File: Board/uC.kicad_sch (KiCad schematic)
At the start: 25 parts, among them U1 STM32F030K6Tx, U4 MP6612

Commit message: Schematic done.
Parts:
- C24: footprint (none) -> Capacitor_SMD:CP_Elec_8x10; REF (none) -> EEH-ZA1V101P
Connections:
- net RXD_TTL: no longer names the net of U1.25 (PA15)
- net TXD_TTL: no longer names the net of U1.24 (PA14)
- net TXEN_TTL: no longer names the net of U1.26 (PB3)
- no-connect marks 14 -> 17
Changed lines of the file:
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@@
+	)
+	(no_connect
+		(at 99.06 125.73)
 	)
 	(no_connect
@@
 	)
 	(no_connect
+		(at 68.58 110.49)
+	)
+	(no_connect
 		(at 68.58 115.57)
 	)
@@
 	(no_connect
 		(at 255.27 48.26)
+	)
+	(no_connect
+		(at 99.06 123.19)
 	)
 	(no_connect
@@
 		)
 	)
-	(global_label "RXD_TTL"
-		(shape input)
-		(at 99.06 125.73 0)
-		(fields_autoplaced yes)
-		(effects
-			(font
-				(size 1.27 1.27)
-			)
-			(justify left)
-		)
-		(property "Intersheetrefs" "${INTERSHEET_REFS}"
-			(at 109.0647 125.6506 0)
-			(effects
-				(font
-					(size 1.27 1.27)
-				)
-				(justify left)
-				(hide yes)
-			)
-		)
-	)
-	(global_label "TXD_TTL"
-		(shape output)
-		(at 99.06 123.19 0)
-		(fields_autoplaced yes)
-		(effects
-			(font
-				(size 1.27 1.27)
-			)
-			(justify left)
-		)
-		(property "Intersheetrefs" "${INTERSHEET_REFS}"
-			(at 108.7623 123.1106 0)
-			(effects
-				(font
-					(size 1.27 1.27)
-				)
-				(justify left)
-				(hide yes)
-			)
-		)
-	)
 	(global_label "HB_nFAULT"
 		(shape output)
@@
 		(property "Intersheetrefs" "${INTERSHEET_REFS}"
 			(at 216.3621 38.1 0)
-			(effects
-				(font
-					(size 1.27 1.27)
-				)
-				(justify right)
-				(hide yes)
-			)
-		)
-	)
-	(global_label "TXEN_TTL"
-		(shape output)
-		(at 68.58 110.49 180)
-		(fields_autoplaced yes)
-		(effects
-			(font
-				(size 1.27 1.27)
-			)
-			(justify right)
-		)
-		(property "Intersheetrefs" "${INTERSHEET_REFS}"
-			(at 57.0073 110.49 0)
 			(effects
 				(font
@@
 			)
 		)
-		(property "Footprint" ""
+		(property "Footprint" "Capacitor_SMD:CP_Elec_8x10"
 			(at 185.42 62.23 0)
 			(effects
@@
 			(at 185.42 62.23 0)
 			(effects
+				(font
+					(size 1.27 1.27)
+				)
+				(hide yes)
+			)
+		)
+		(property "REF" "EEH-ZA1V101P"
+			(at 185.42 62.23 0)
+			(effects

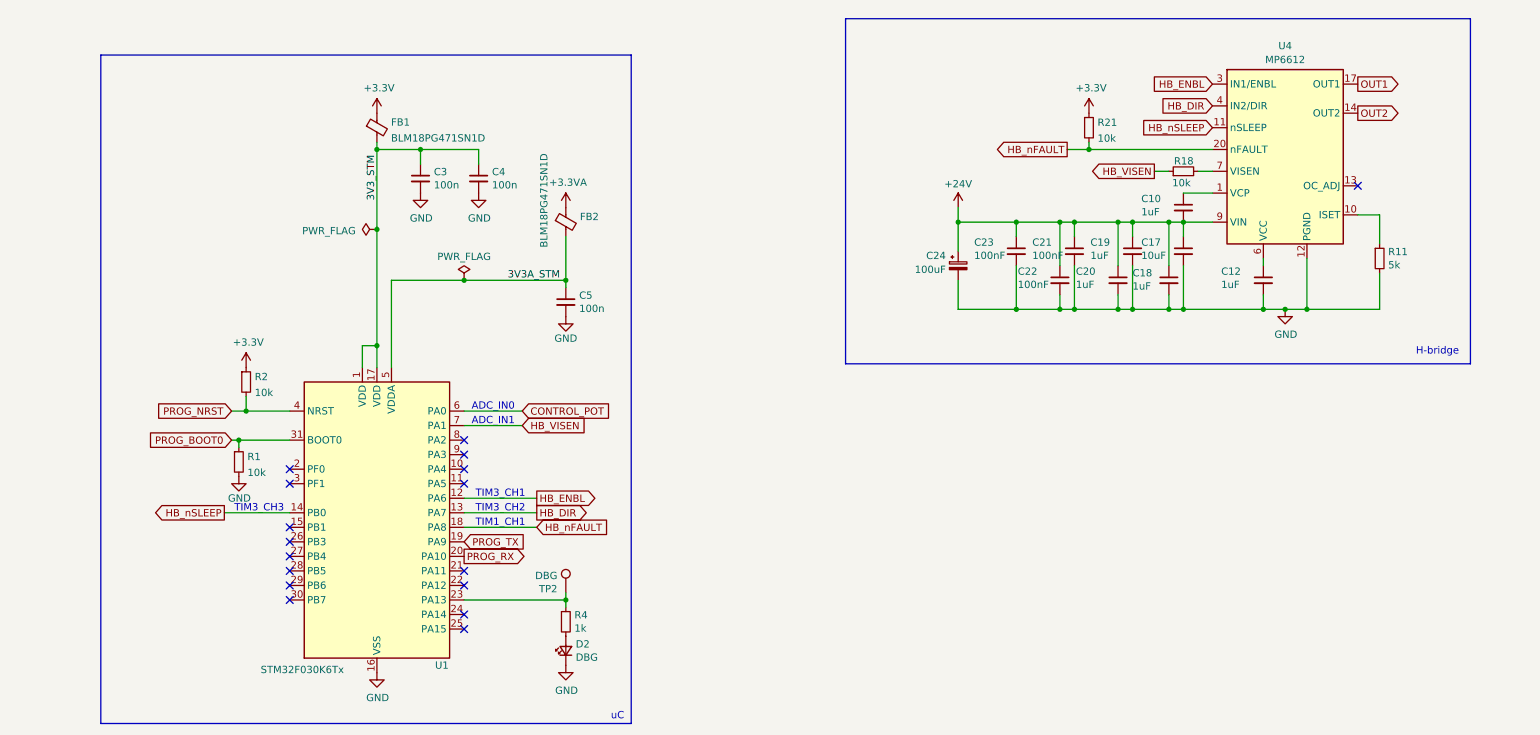
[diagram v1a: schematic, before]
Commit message: Included jdam's improvements.
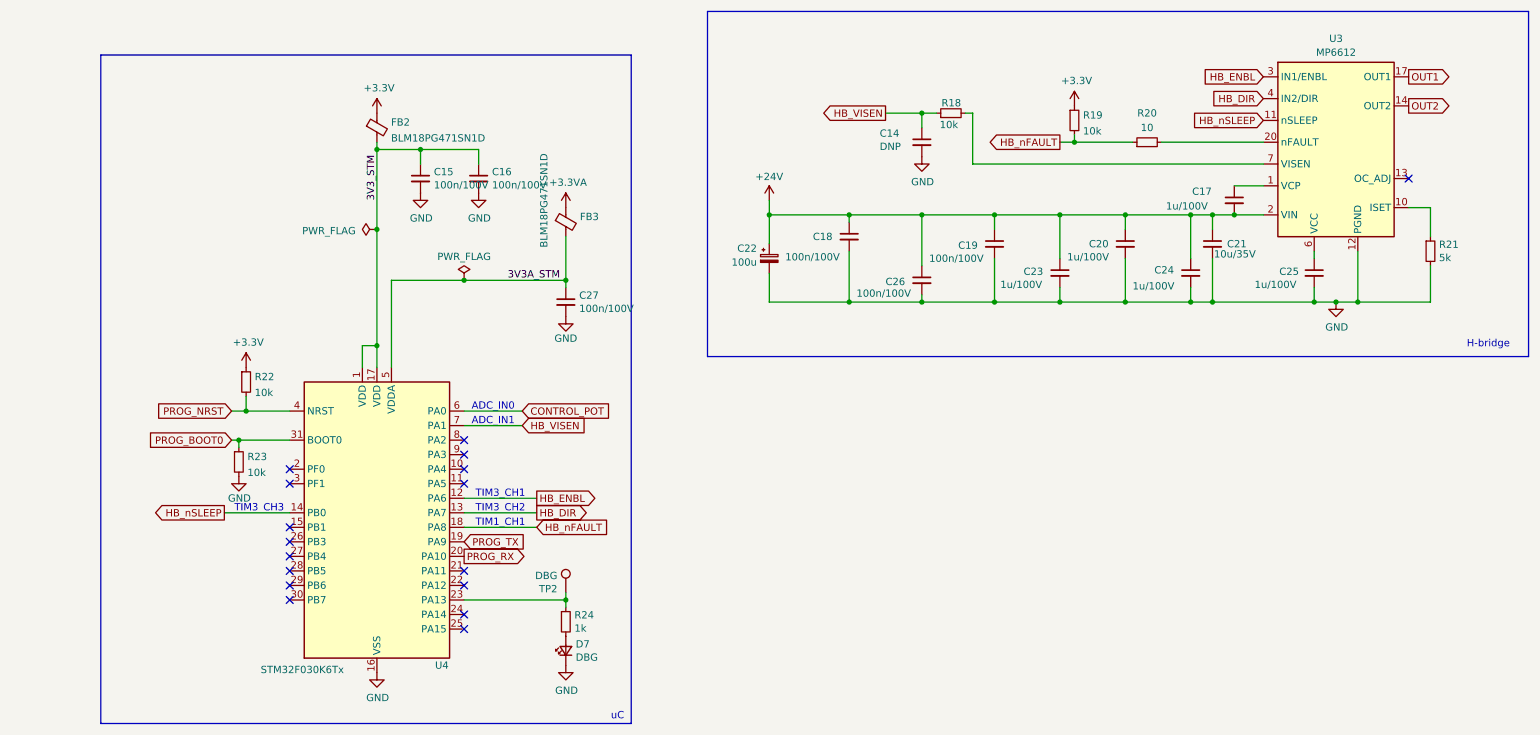
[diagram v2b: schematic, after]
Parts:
- added C14: DNP, Capacitor_SMD:C_0603_1608Metric_Pad1.08x0.95mm_HandSolder, symbol Device:C_Small
- added R20: 10, Resistor_SMD:R_0603_1608Metric_Pad0.98x0.95mm_HandSolder, symbol Device:R_Small
- C15: renamed from C3; value 100n -> 100n/100V; footprint Capacitor_SMD:C_0603_1608Metric -> Capacitor_SMD:C_0603_1608Metric_Pad1.08x0.95mm_HandSolder
- C16: renamed from C4; value 100n -> 100n/100V; footprint Capacitor_SMD:C_0603_1608Metric -> Capacitor_SMD:C_0603_1608Metric_Pad1.08x0.95mm_HandSolder
- C17: renamed from C10; value 1uF -> 1u/100V; footprint Capacitor_SMD:C_0603_1608Metric -> Capacitor_SMD:C_0603_1608Metric_Pad1.08x0.95mm_HandSolder
- C18: renamed from C23; value 100nF -> 100n/100V; footprint Capacitor_SMD:C_0603_1608Metric -> Capacitor_SMD:C_0603_1608Metric_Pad1.08x0.95mm_HandSolder
- C19: renamed from C21; value 100nF -> 100n/100V; footprint Capacitor_SMD:C_0603_1608Metric -> Capacitor_SMD:C_0603_1608Metric_Pad1.08x0.95mm_HandSolder
- C20: renamed from C19; value 1uF -> 1u/100V; footprint Capacitor_SMD:C_0603_1608Metric -> Capacitor_SMD:C_0603_1608Metric_Pad1.08x0.95mm_HandSolder
- C21: renamed from C17; value 10uF -> 10u/35V; footprint Capacitor_SMD:C_0603_1608Metric -> Capacitor_SMD:C_0603_1608Metric_Pad1.08x0.95mm_HandSolder
- C22: renamed from C24; value 100uF -> 100u
- C23: renamed from C20; value 1uF -> 1u/100V; footprint Capacitor_SMD:C_0603_1608Metric -> Capacitor_SMD:C_0603_1608Metric_Pad1.08x0.95mm_HandSolder
- C24: renamed from C18; value 1uF -> 1u/100V; footprint Capacitor_SMD:C_0603_1608Metric -> Capacitor_SMD:C_0603_1608Metric_Pad1.08x0.95mm_HandSolder
- C25: renamed from C12; value 1uF -> 1u/100V; footprint Capacitor_SMD:C_0603_1608Metric -> Capacitor_SMD:C_0603_1608Metric_Pad1.08x0.95mm_HandSolder
- C26: renamed from C22; value 100nF -> 100n/100V; footprint Capacitor_SMD:C_0603_1608Metric -> Capacitor_SMD:C_0603_1608Metric_Pad1.08x0.95mm_HandSolder
- C27: renamed from C5; value 100n -> 100n/100V; footprint Capacitor_SMD:C_0603_1608Metric -> Capacitor_SMD:C_0603_1608Metric_Pad1.08x0.95mm_HandSolder
- R18: footprint Resistor_SMD:R_0603_1608Metric -> Resistor_SMD:R_0603_1608Metric_Pad0.98x0.95mm_HandSolder
- R19: renamed from R21; footprint Resistor_SMD:R_0603_1608Metric -> Resistor_SMD:R_0603_1608Metric_Pad0.98x0.95mm_HandSolder
- R21: renamed from R11; footprint Resistor_SMD:R_0603_1608Metric -> Resistor_SMD:R_0603_1608Metric_Pad0.98x0.95mm_HandSolder
- R22: renamed from R2; footprint Resistor_SMD:R_0603_1608Metric -> Resistor_SMD:R_0603_1608Metric_Pad0.98x0.95mm_HandSolder
- R23: renamed from R1; footprint Resistor_SMD:R_0603_1608Metric -> Resistor_SMD:R_0603_1608Metric_Pad0.98x0.95mm_HandSolder
- R24: renamed from R4; footprint Resistor_SMD:R_0603_1608Metric -> Resistor_SMD:R_0603_1608Metric_Pad0.98x0.95mm_HandSolder
- renumbered D2 to D7, FB1 to FB2, FB2 to FB3, U4 to U3, U1 to U4
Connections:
- net HB_VISEN: now also C14.1
- net HB_nFAULT: now also R20.1; no longer U3.20 (nFAULT)
- net AGND renamed GND
- net GND: now also C14.2
- new net: R20.2, U3.20 (nFAULT)
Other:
- moved on the sheet: C17, C18, C19, C20, C21, C22, C23, C24, C25, C26, R18, R19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

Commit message: WIP on routing
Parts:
- removed D7: DBG, LED_SMD:LED_0603_1608Metric, symbol Device:LED_Small
- removed R24: 1k, Resistor_SMD:R_0603_1608Metric_Pad0.98x0.95mm_HandSolder, symbol Device:R_Small
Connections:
- net HB_VISEN: now also U4.8 (PA2); no longer U4.7 (PA1)
- net STATUS_LED: now reaches TP2.1, U4.23 (PA13)
- new net POSITION_POT: U4.7 (PA1)
- no-connect marks 17 -> 16
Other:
- note added: "ADC_IN2"
- moved on the sheet: C15, C16, C27, FB2, FB3, R22, R23, TP2, U4

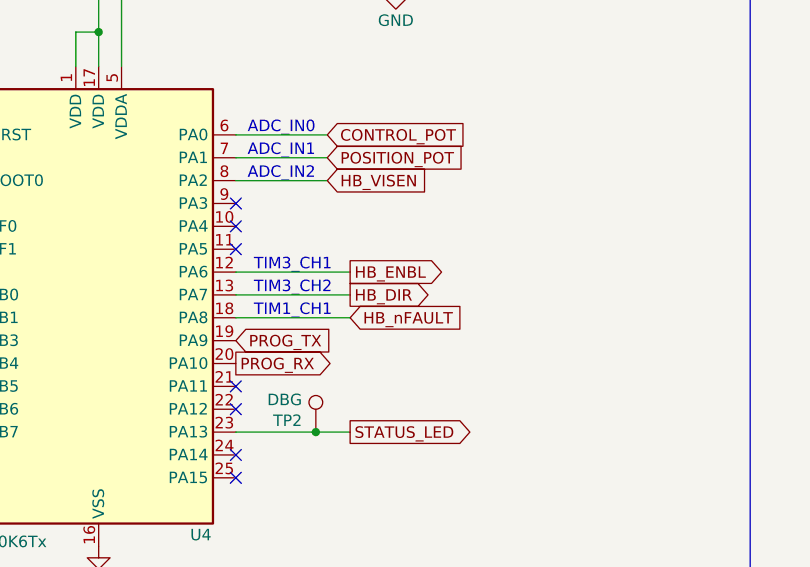
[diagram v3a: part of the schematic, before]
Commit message: Routing done, before adding polyfuse
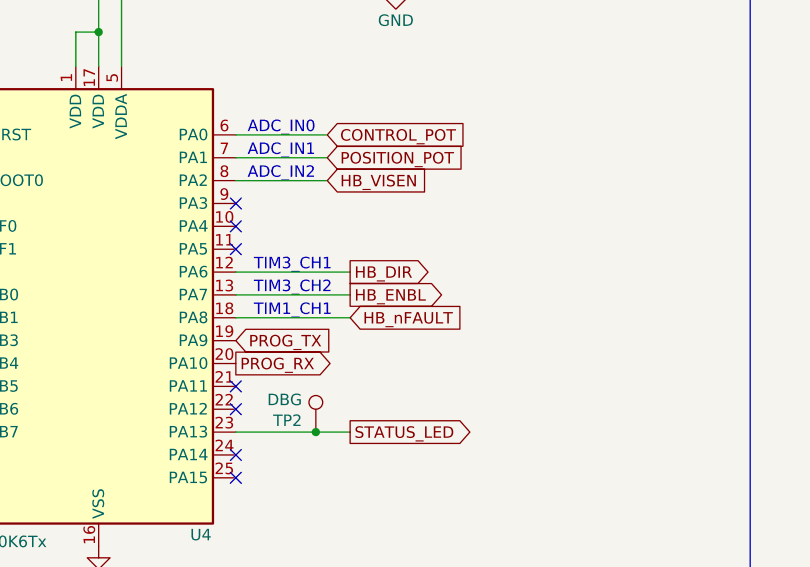
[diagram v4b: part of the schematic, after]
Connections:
- net HB_DIR: now also U4.12 (PA6); no longer U4.13 (PA7)
- net HB_ENBL: now also U4.13 (PA7); no longer U4.12 (PA6)

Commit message: Silkscreen done.
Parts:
- renumbered C23 to C1, C25 to C10, C21 to C11, C16 to C12, C15 to C13, C27 to C17, C26 to C2, C14 to C24, C17 to C3, C22 to C4, C20 to C5, C19 to C6, C24 to C7, C18 to C8, FB2 to FB1, FB3 to FB2, R22 to R11, R20 to R18, R18 to R21, R21 to R6, R23 to R7, TP2 to TP1, U3 to U1, U4 to U3
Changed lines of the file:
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@@
 		(on_board yes)
 		(dnp no)
-		(property "Reference" "C19"
+		(property "Reference" "C6"
 			(at 185.42 58.674 0)
 			(effects
@@
 			(project "linear_act_controller"
 				(path "/a7f12679-28d2-4dcb-a620-9ebf42b92b51/db8eb4c5-25c6-41a9-b739-ec315f7b77a5"
-					(reference "C19")
+					(reference "C6")
 					(unit 1)
 				)
@@
 		(on_board yes)
 		(dnp no)
-		(property "Reference" "C26"
+		(property "Reference" "C2"
 			(at 172.72 65.024 0)
 			(effects
@@
 			(project "linear_act_controller"
 				(path "/a7f12679-28d2-4dcb-a620-9ebf42b92b51/db8eb4c5-25c6-41a9-b739-ec315f7b77a5"
-					(reference "C26")
+					(reference "C2")
 					(unit 1)
 				)
@@
 		(dnp no)
 		(fields_autoplaced yes)
-		(property "Reference" "R20"
+		(property "Reference" "R18"
 			(at 218.44 35.56 90)
 			(effects
@@
 			(project "linear_act_controller"
 				(path "/a7f12679-28d2-4dcb-a620-9ebf42b92b51/db8eb4c5-25c6-41a9-b739-ec315f7b77a5"
-					(reference "R20")
+					(reference "R18")
 					(unit 1)
 				)
@@
 		(on_board yes)
 		(dnp no)
-		(property "Reference" "C25"
+		(property "Reference" "C10"
 			(at 241.554 63.246 0)
 			(effects
@@
 			(project "linear_act_controller"
 				(path "/a7f12679-28d2-4dcb-a620-9ebf42b92b51/db8eb4c5-25c6-41a9-b739-ec315f7b77a5"
-					(reference "C25")
+					(reference "C10")
 					(unit 1)
 				)
@@
 		(on_board yes)
 		(dnp no)
-		(property "Reference" "FB3"
+		(property "Reference" "FB2"
 			(at 97.7138 49.8534 0)
 			(effects
@@
 			(project "linear_act_controller"
 				(path "/a7f12679-28d2-4dcb-a620-9ebf42b92b51/db8eb4c5-25c6-41a9-b739-ec315f7b77a5"
-					(reference "FB3")
+					(reference "FB2")
 					(unit 1)
 				)
@@
 		(dnp no)
 		(fields_autoplaced yes)
-		(property "Reference" "U3"
+		(property "Reference" "U1"
 			(at 251.46 22.5255 0)
 			(effects
@@
 			(project ""
 				(path "/a7f12679-28d2-4dcb-a620-9ebf42b92b51/db8eb4c5-25c6-41a9-b739-ec315f7b77a5"
-					(reference "U3")
+					(reference "U1")
 					(unit 1)
 				)
@@
 		(on_board yes)
 		(dnp no)
-		(property "Reference" "U4"
+		(property "Reference" "U3"
 			(at 72.39 128.27 0)
 			(effects
@@
 			(project "linear_act_controller"
 				(path "/a7f12679-28d2-4dcb-a620-9ebf42b92b51/db8eb4c5-25c6-41a9-b739-ec315f7b77a5"
-					(reference "U4")
+					(reference "U3")
 					(unit 1)
 				)
@@
 		(on_board yes)
 		(dnp no)
-		(property "Reference" "C22"
+		(property "Reference" "C4"
 			(at 150.241 59.2017 0)
 			(effects
@@
 			(project ""
 				(path "/a7f12679-28d2-4dcb-a620-9ebf42b92b51/db8eb4c5-25c6-41a9-b739-ec315f7b77a5"
-					(reference "C22")
+					(reference "C4")
 					(unit 1)
 				)
@@
 		(on_board yes)
 		(dnp no)
-		(property "Reference" "C20"
+		(property "Reference" "C5"
 			(at 208.28 58.42 0)
 			(effects
@@
 			(project "linear_act_controller"
 				(path "/a7f12679-28d2-4dcb-a620-9ebf42b92b51/db8eb4c5-25c6-41a9-b739-ec315f7b77a5"
-					(reference "C20")
+					(reference "C5")
 					(unit 1)
 				)
@@
 		(on_board yes)
 		(dnp no)
-		(property "Reference" "C27"
+		(property "Reference" "C17"
 			(at 97.5868 63.6016 0)
 			(effects
@@
 			(project "linear_act_controller"
 				(path "/a7f12679-28d2-4dcb-a620-9ebf42b92b51/db8eb4c5-25c6-41a9-b739-ec315f7b77a5"
-					(reference "C27")
+					(reference "C17")
 					(unit 1)
 				)
@@
 		(dnp no)
 		(fields_autoplaced yes)
-		(property "Reference" "R22"
+		(property "Reference" "R11"
 			(at 40.8686 77.8315 0)
 			(effects
@@
 			(project "linear_act_controller"
 				(path "/a7f12679-28d2-4dcb-a620-9ebf42b92b51/db8eb4c5-25c6-41a9-b739-ec315f7b77a5"
-					(reference "R22")
+					(reference "R11")
 					(unit 1)
 				)
@@
 		(on_board yes)
 		(dnp no)
-		(property "Reference" "C23"
+		(property "Reference" "C1"
 			(at 196.85 63.246 0)
 			(effects
@@
 			(project "linear_act_controller"
 				(path "/a7f12679-28d2-4dcb-a620-9ebf42b92b51/db8eb4c5-25c6-41a9-b739-ec315f7b77a5"
-					(reference "C23")
+					(reference "C1")
 					(unit 1)
 				)
@@
 		(dnp no)
 		(fields_autoplaced yes)
-		(property "Reference" "FB2"
+		(property "Reference" "FB1"
 			(at 64.6938 33.3434 0)
 			(effects
@@
 			(project "linear_act_controller"
 				(path "/a7f12679-28d2-4dcb-a620-9ebf42b92b51/db8eb4c5-25c6-41a9-b739-ec315f7b77a5"
-					(reference "FB2")
+					(reference "FB1")
 					(unit 1)
 				)
@@
 		(on_board yes)
 		(dnp no)
-		(property "Reference" "C21"
+		(property "Reference" "C11"
 			(at 232.41 58.42 0)
 			(effects
@@
 			(project "linear_act_controller"
 				(path "/a7f12679-28d2-4dcb-a620-9ebf42b92b51/db8eb4c5-25c6-41a9-b739-ec315f7b77a5"
-					(reference "C21")
+					(reference "C11")
 					(unit 1)
 				)
@@
 		(on_board yes)
 		(dnp no)
-		(property "Reference" "C24"
+		(property "Reference" "C7"
 			(at 219.71 62.992 0)
 			(effects
@@
 			(project "linear_act_controller"
 				(path "/a7f12679-28d2-4dcb-a620-9ebf42b92b51/db8eb4c5-25c6-41a9-b739-ec315f7b77a5"
-					(reference "C24")
+					(reference "C7")
 					(unit 1)
 				)
@@
 		(on_board yes)
 		(dnp no)
-		(property "Reference" "R21"
+		(property "Reference" "R6"
 			(at 269.4686 58.5216 0)
 			(effects
@@
 			(project "linear_act_controller"
 				(path "/a7f12679-28d2-4dcb-a620-9ebf42b92b51/db8eb4c5-25c6-41a9-b739-ec315f7b77a5"
-					(reference "R21")
+					(reference "R6")
 					(unit 1)
 				)
@@
 		(on_board yes)
 		(dnp no)
-		(property "Reference" "TP2"
+		(property "Reference" "TP1"
 			(at 84.836 115.57 0)
 			(effects
@@
 			(project "linear_act_controller"
 				(path "/a7f12679-28d2-4dcb-a620-9ebf42b92b51/db8eb4c5-25c6-41a9-b739-ec315f7b77a5"
-					(reference "TP2")
+					(reference "TP1")
 					(unit 1)
 				)
@@
 		(on_board yes)
 		(dnp no)
-		(property "Reference" "C17"
+		(property "Reference" "C3"
 			(at 226.314 49.2506 0)
 			(effects
@@
 			(project "linear_act_controller"
 				(path "/a7f12679-28d2-4dcb-a620-9ebf42b92b51/db8eb4c5-25c6-41a9-b739-ec315f7b77a5"
-					(reference "C17")
+					(reference "C3")
 					(unit 1)
 				)
@@
 		(on_board yes)
 		(dnp no)
-		(property "Reference" "C16"
+		(property "Reference" "C12"
 			(at 82.3468 42.0116 0)
 			(effects
@@
 			(project "linear_act_controller"
 				(path "/a7f12679-28d2-4dcb-a620-9ebf42b92b51/db8eb4c5-25c6-41a9-b739-ec315f7b77a5"
-					(reference "C16")
+					(reference "C12")
 					(unit 1)
 				)
@@
 		(on_board yes)
 		(dnp no)
-		(property "Reference" "R18"
+		(property "Reference" "R21"
 			(at 185.928 33.782 90)
 			(effects
@@
 			(project "linear_act_controller"
 				(path "/a7f12679-28d2-4dcb-a620-9ebf42b92b51/db8eb4c5-25c6-41a9-b739-ec315f7b77a5"
-					(reference "R18")
+					(reference "R21")
 					(unit 1)
 				)
@@
 		(on_board yes)
 		(dnp no)
-		(property "Reference" "C14"
+		(property "Reference" "C24"
 			(at 171.704 39.0906 0)
 			(effects
@@
 			(project "linear_act_controller"
 				(path "/a7f12679-28d2-4dcb-a620-9ebf42b92b51/db8eb4c5-25c6-41a9-b739-ec315f7b77a5"
-					(reference "C14")
+					(reference "C24")
 					(unit 1)
 				)
@@
 		(on_board yes)
 		(dnp no)
-		(property "Reference" "C15"
+		(property "Reference" "C13"
 			(at 72.1868 42.0116 0)
 			(effects
@@
 			(project "linear_act_controller"
 				(path "/a7f12679-28d2-4dcb-a620-9ebf42b92b51/db8eb4c5-25c6-41a9-b739-ec315f7b77a5"
-					(reference "C15")
+					(reference "C13")
 					(unit 1)
 				)
@@
 		(dnp no)
 		(fields_autoplaced yes)
-		(property "Reference" "R23"
+		(property "Reference" "R7"
 			(at 39.5986 91.8015 0)
 			(effects
@@
 			(project "linear_act_controller"
 				(path "/a7f12679-28d2-4dcb-a620-9ebf42b92b51/db8eb4c5-25c6-41a9-b739-ec315f7b77a5"
-					(reference "R23")
+					(reference "R7")
 					(unit 1)
 				)
@@
 		(on_board yes)
 		(dnp no)
-		(property "Reference" "C18"
+		(property "Reference" "C8"
 			(at 160.02 57.15 0)
 			(effects
@@
 			(project "linear_act_controller"
 				(path "/a7f12679-28d2-4dcb-a620-9ebf42b92b51/db8eb4c5-25c6-41a9-b739-ec315f7b77a5"
-					(reference "C18")
-					(unit 1)
-				)
+					(reference "C8")
+					(unit 1)
+				)
